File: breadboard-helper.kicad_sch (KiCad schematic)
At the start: 4 parts, among them J1 POWER_A_1, J2 POWER_B_1, J3 POWER_A_2, J4 POWER_B_2

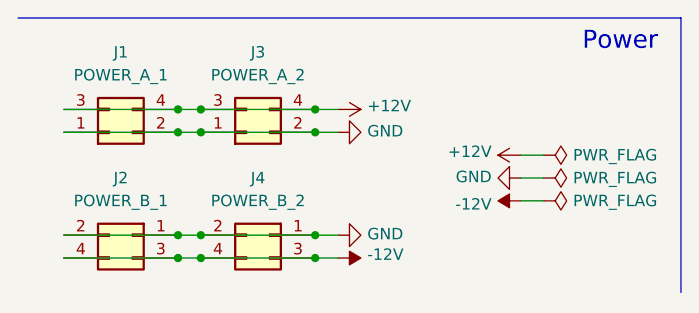
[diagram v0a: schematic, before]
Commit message: Add 1N5819HW diodes for reverse polarity protection
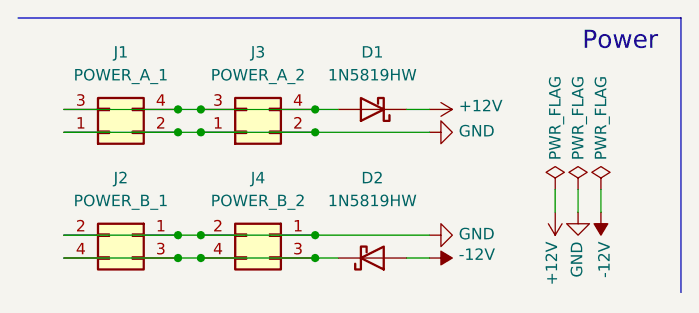
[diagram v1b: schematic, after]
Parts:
- added D1, D2: 1N5819HW, Diode_SMD:D_SOD-123, symbol Device:D_Schottky
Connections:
- net +12V: now also D1.1 (K); no longer J1.3 (Pin_3), J1.4 (Pin_4), J3.3 (Pin_3), J3.4 (Pin_4)
- net -12V: now also D2.2 (A); no longer J2.3 (Pin_3), J2.4 (Pin_4), J4.3 (Pin_3), J4.4 (Pin_4)
- new net: D2.1 (K), J2.3 (Pin_3), J2.4 (Pin_4), J4.3 (Pin_3), J4.4 (Pin_4)
- new net: D1.2 (A), J1.3 (Pin_3), J1.4 (Pin_4), J3.3 (Pin_3), J3.4 (Pin_4)
